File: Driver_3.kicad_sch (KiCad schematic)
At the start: 34 parts

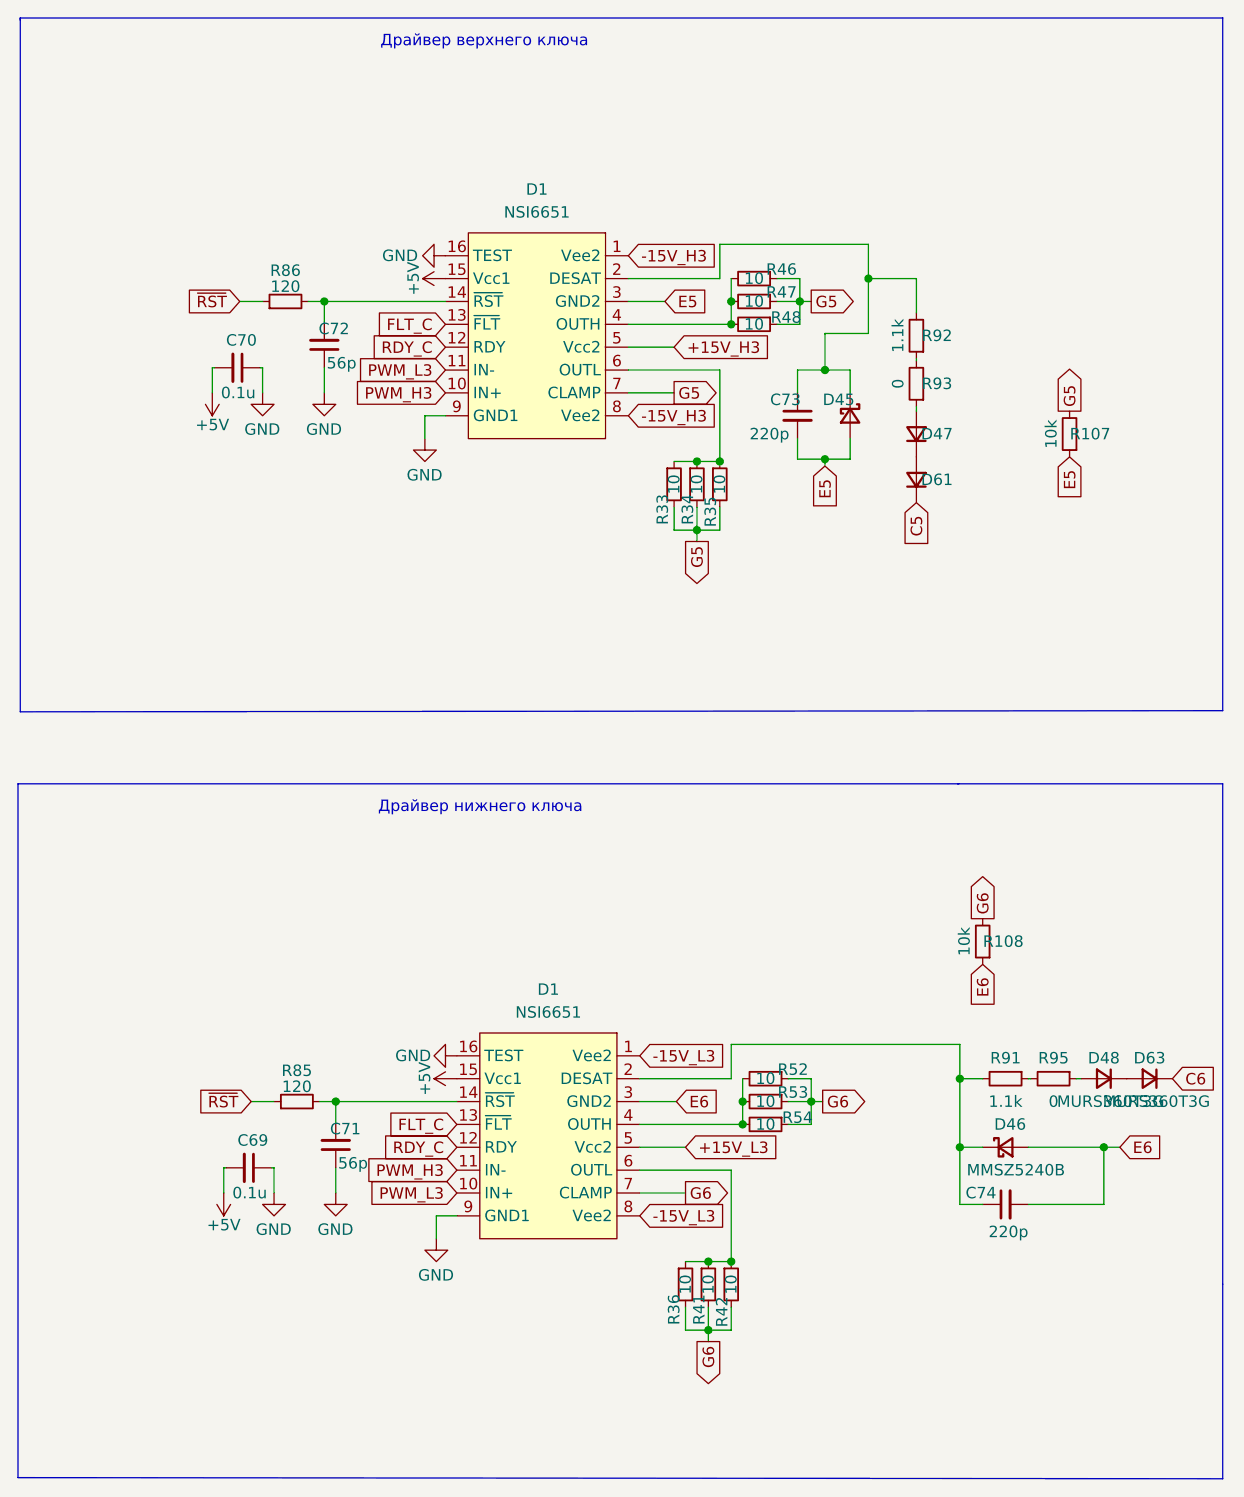
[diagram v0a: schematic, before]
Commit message: Отправил на проверку в резонит: изменил BOM
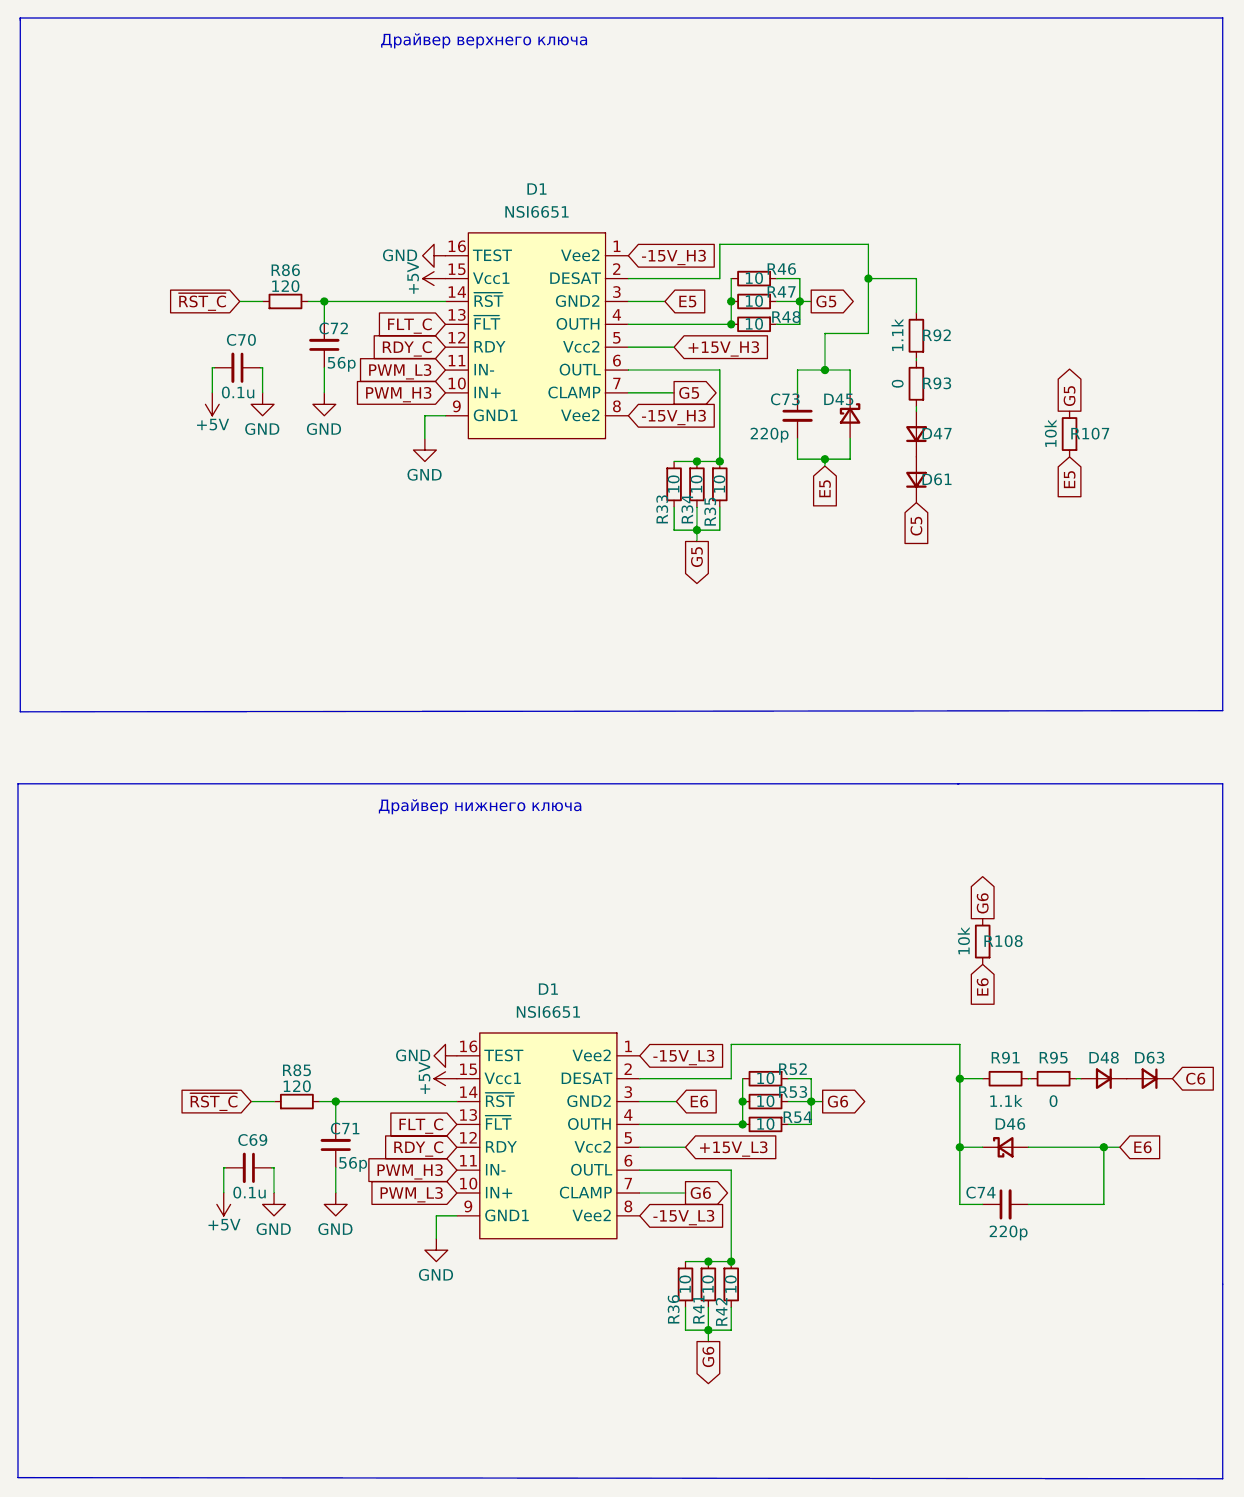
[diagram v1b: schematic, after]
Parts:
- D47, D48, D61, D63: value MURS360T3G -> MURS160
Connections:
- net ~{RST} renamed ~{RST_C}
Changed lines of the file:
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@@
 		)
 	)
-	(global_label "~{RST}"
-		(shape input)
-		(at 55.88 54.61 180)
-		(fields_autoplaced yes)
-		(effects
-			(font
-				(size 1.27 1.27)
-			)
-			(justify right)
-		)
-		(property "Intersheetrefs" "${INTERSHEET_REFS}"
-			(at 50.065 54.61 0)
-			(effects
-				(font
-					(size 1.27 1.27)
-				)
-				(justify right)
-				(hide yes)
-			)
-		)
-	)
 	(global_label "G6"
 		(shape output)
@@
 		)
 	)
-	(global_label "~{RST}"
-		(shape input)
-		(at 57.15 143.51 180)
-		(fields_autoplaced yes)
-		(effects
-			(font
-				(size 1.27 1.27)
-			)
-			(justify right)
-		)
-		(property "Intersheetrefs" "${INTERSHEET_REFS}"
-			(at 51.335 143.51 0)
-			(effects
-				(font
-					(size 1.27 1.27)
-				)
-				(justify right)
-				(hide yes)
-			)
-		)
-	)
 	(global_label "-15V_L3"
 		(shape input)
@@
 		)
 	)
+	(global_label "~{RST_C}"
+		(shape input)
+		(at 55.88 54.61 180)
+		(fields_autoplaced yes)
+		(effects
+			(font
+				(size 1.27 1.27)
+			)
+			(justify right)
+		)
+		(property "Intersheetrefs" "${INTERSHEET_REFS}"
+			(at 47.2101 54.61 0)
+			(effects
+				(font
+					(size 1.27 1.27)
+				)
+				(justify right)
+				(hide yes)
+			)
+		)
+	)
 	(global_label "PWM_H3"
 		(shape input)
@@
 		)
 	)
+	(global_label "~{RST_C}"
+		(shape input)
+		(at 57.15 143.51 180)
+		(fields_autoplaced yes)
+		(effects
+			(font
+				(size 1.27 1.27)
+			)
+			(justify right)
+		)
+		(property "Intersheetrefs" "${INTERSHEET_REFS}"
+			(at 48.4801 143.51 0)
+			(effects
+				(font
+					(size 1.27 1.27)
+				)
+				(justify right)
+				(hide yes)
+			)
+		)
+	)
 	(global_label "+15V_H3"
 		(shape input)
@@
 			)
 		)
-		(property "Value" "MURS360T3G"
+		(property "Value" "MURS160"
 			(at 152.654 143.51 0)
 			(effects
@@
 					(size 1.27 1.27)
 				)
+				(hide yes)
 			)
 		)
@@
 			)
 		)
-		(property "Value" "MURS360T3G"
+		(property "Value" "MURS160"
 			(at 128.524 70.104 0)
 			(effects
@@
 			)
 		)
-		(property "Value" "MURS360T3G"
+		(property "Value" "MURS160"
 			(at 157.734 143.51 0)
 			(effects
@@
 					(size 1.27 1.27)
 				)
+				(hide yes)
 			)
 		)
@@
 				)
 				(justify left)
+				(hide yes)
 			)
 		)
@@
 			)
 		)
-		(property "Value" "MURS360T3G"
+		(property "Value" "MURS160"
 			(at 128.524 75.184 0)
 			(effects

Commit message: Изменения: обновил BOM и названия в схеме
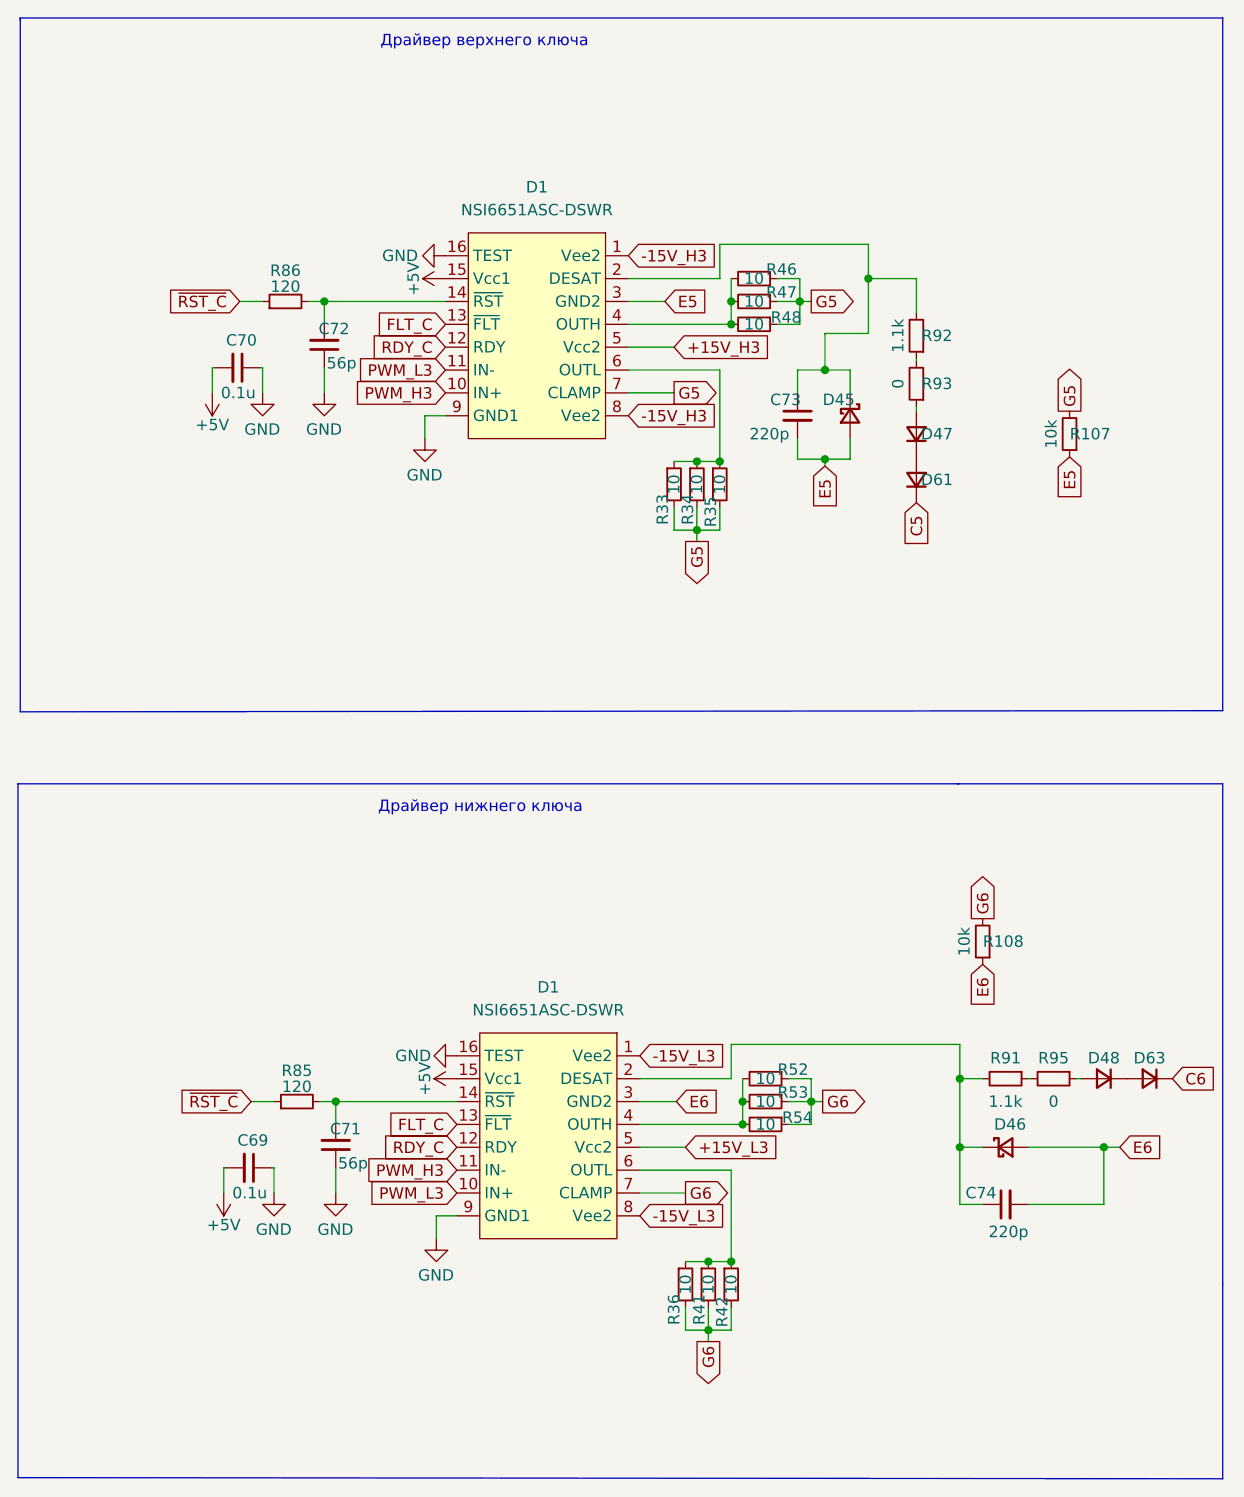
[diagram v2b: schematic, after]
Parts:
- D1: value NSI6651 -> NSI6651ASC-DSWR
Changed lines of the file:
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@@
 		(fields_autoplaced yes)
 		(property "Reference" "D1"
-			(at 88.9 42.164 0)
+			(at 88.9 41.91 0)
 			(effects
 				(font
@@
 			)
 		)
-		(property "Value" "NSI6651"
-			(at 88.9 44.704 0)
+		(property "Value" "NSI6651ASC-DSWR"
+			(at 88.9 44.45 0)
 			(effects
 				(font
@@
 		(fields_autoplaced yes)
 		(property "Reference" "D1"
-			(at 90.17 131.064 0)
+			(at 90.17 130.81 0)
 			(effects
 				(font
@@
 			)
 		)
-		(property "Value" "NSI6651"
-			(at 90.17 133.604 0)
+		(property "Value" "NSI6651ASC-DSWR"
+			(at 90.17 133.35 0)
 			(effects
 				(font

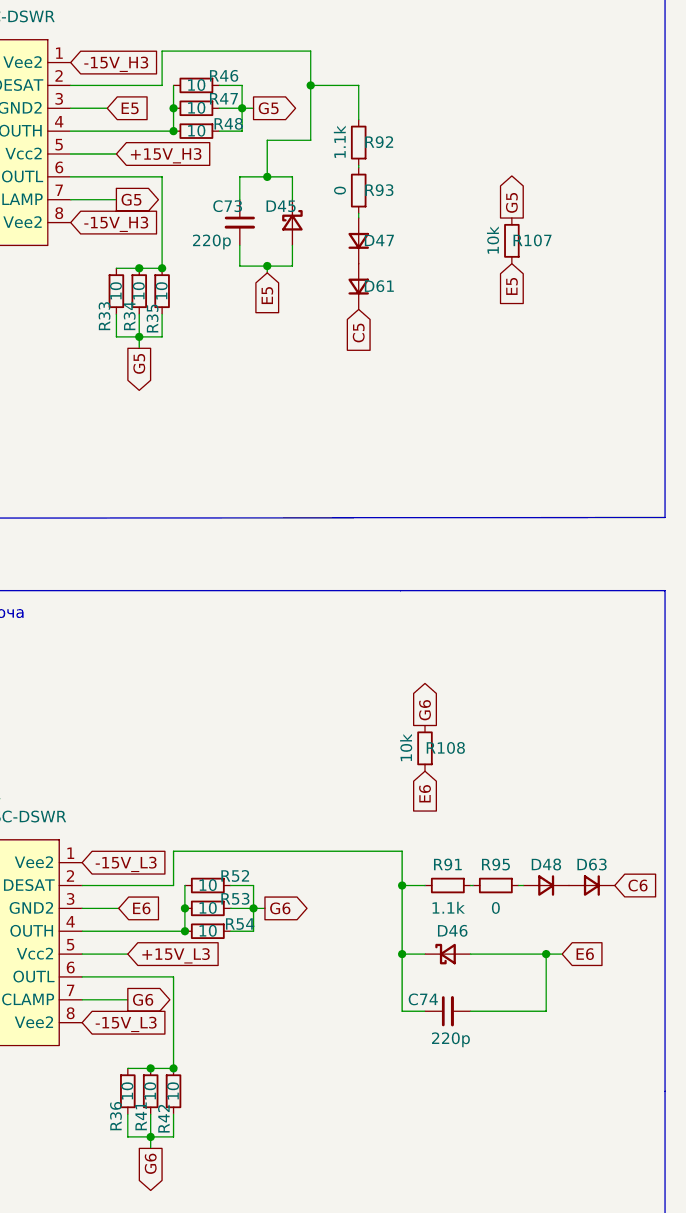
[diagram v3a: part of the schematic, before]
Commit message: Изменения: поменял трассировку полигонов, изменил трассировку цепи DESAT в фазе А
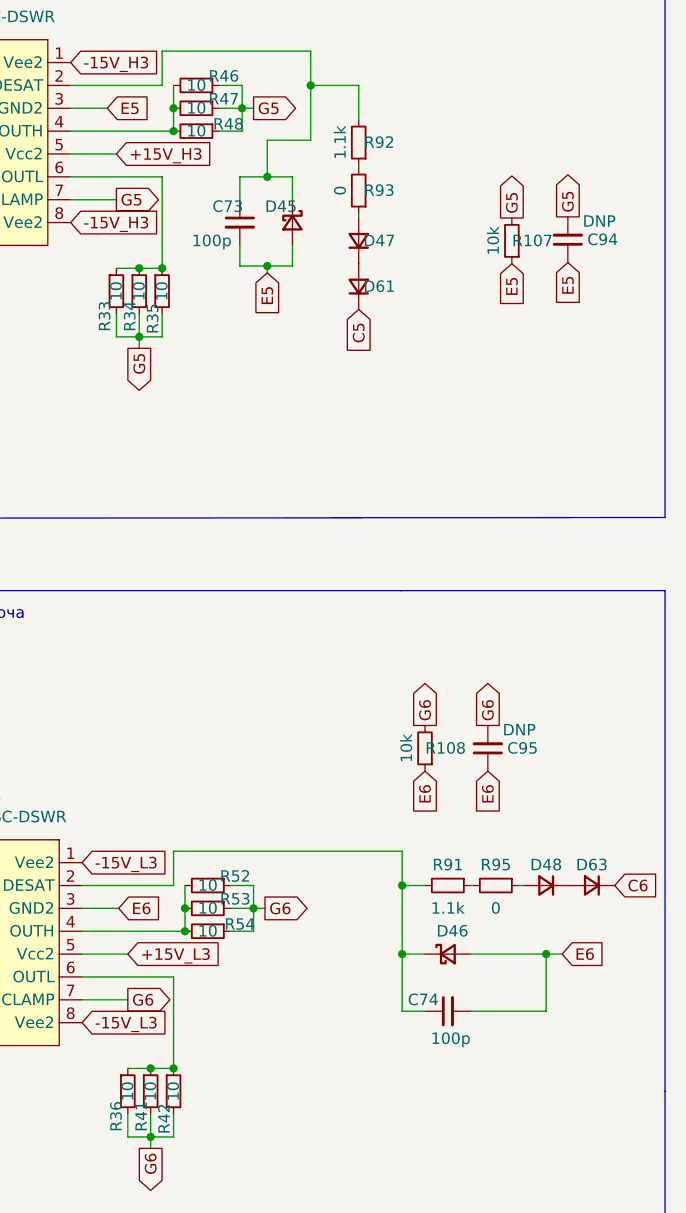
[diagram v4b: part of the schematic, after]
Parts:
- added C94, C95: DNP, Capacitor_SMD:C_0805_2012Metric_Pad1.18x1.45mm_HandSolder, symbol Device:C_Small
- C73, C74: value 220p -> 100p
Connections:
- net E5: now also C94.1
- net E6: now also C95.1
- net G5: now also C94.2
- net G6: now also C95.2
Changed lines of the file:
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@@
+		)
+	)
+	(global_label "G5"
+		(shape output)
+		(at 154.305 66.675 90)
+		(fields_autoplaced yes)
+		(effects
+			(font
+				(size 1.27 1.27)
+			)
+			(justify left)
+		)
+		(property "Intersheetrefs" "${INTERSHEET_REFS}"
+			(at 154.2256 61.7824 90)
+			(effects
+				(font
+					(size 1.27 1.27)
+				)
+				(justify left)
+				(hide yes)
+			)
 		)
 	)
@@
 		)
 	)
+	(global_label "G6"
+		(shape output)
+		(at 145.415 123.19 90)
+		(fields_autoplaced yes)
+		(effects
+			(font
+				(size 1.27 1.27)
+			)
+			(justify left)
+		)
+		(property "Intersheetrefs" "${INTERSHEET_REFS}"
+			(at 145.3356 118.2974 90)
+			(effects
+				(font
+					(size 1.27 1.27)
+				)
+				(justify left)
+				(hide yes)
+			)
+		)
+	)
 	(global_label "RDY_C"
 		(shape input)
@@
 		)
 	)
+	(global_label "E5"
+		(shape input)
+		(at 154.305 71.755 270)
+		(fields_autoplaced yes)
+		(effects
+			(font
+				(size 1.27 1.27)
+			)
+			(justify right)
+		)
+		(property "Intersheetrefs" "${INTERSHEET_REFS}"
+			(at 154.2256 76.5267 90)
+			(effects
+				(font
+					(size 1.27 1.27)
+				)
+				(justify right)
+				(hide yes)
+			)
+		)
+	)
 	(global_label "G6"
 		(shape output)
@@
 		)
 	)
+	(global_label "E6"
+		(shape input)
+		(at 145.415 128.27 270)
+		(fields_autoplaced yes)
+		(effects
+			(font
+				(size 1.27 1.27)
+			)
+			(justify right)
+		)
+		(property "Intersheetrefs" "${INTERSHEET_REFS}"
+			(at 145.3356 133.0417 90)
+			(effects
+				(font
+					(size 1.27 1.27)
+				)
+				(justify right)
+				(hide yes)
+			)
+		)
+	)
 	(global_label "G5"
 		(shape output)
@@
 	)
 	(symbol
+		(lib_id "Device:C_Small")
+		(at 145.415 125.73 180)
+		(unit 1)
+		(exclude_from_sim no)
+		(in_bom yes)
+		(on_board yes)
+		(dnp no)
+		(property "Reference" "C95"
+			(at 151.003 125.73 0)
+			(effects
+				(font
+					(size 1.27 1.27)
+				)
+				(justify left)
+			)
+		)
+		(property "Value" "DNP"
+			(at 150.749 123.698 0)
+			(effects
+				(font
+					(size 1.27 1.27)
+				)
+				(justify left)
+			)
+		)
+		(property "Footprint" "Capacitor_SMD:C_0805_2012Metric_Pad1.18x1.45mm_HandSolder"
+			(at 145.415 125.73 0)
+			(effects
+				(font
+					(size 1.27 1.27)
+				)
+				(hide yes)
+			)
+		)
+		(property "Datasheet" "~"
+			(at 145.415 125.73 0)
+			(effects
+				(font
+					(size 1.27 1.27)
+				)
+				(hide yes)
+			)
+		)
+		(property "Description" "Unpolarized capacitor, small symbol"
+			(at 145.415 125.73 0)
+			(effects
+				(font
+					(size 1.27 1.27)
+				)
+				(hide yes)
+			)
+		)
+		(pin "1"
+		)
+		(pin "2"
+		)
+		(instances
+			(project "Adapter"
+				(path "/e63e39d7-6ac0-4ffd-8aa3-1841a4541b55/4f6bfb91-7e0a-4b8d-9918-082ff107cb6c"
+					(reference "C95")
+					(unit 1)
+				)
+			)
+		)
+	)
+	(symbol
 		(lib_id "Device:R_Small")
 		(at 105.41 163.83 0)
@@
 			)
 		)
-		(property "Value" "220p"
+		(property "Value" "100p"
 			(at 112.522 69.342 0)
 			(effects
@@
 	)
 	(symbol
+		(lib_id "Device:C_Small")
+		(at 154.305 69.215 180)
+		(unit 1)
+		(exclude_from_sim no)
+		(in_bom yes)
+		(on_board yes)
+		(dnp no)
+		(property "Reference" "C94"
+			(at 159.893 69.215 0)
+			(effects
+				(font
+					(size 1.27 1.27)
+				)
+				(justify left)
+			)
+		)
+		(property "Value" "DNP"
+			(at 159.639 67.183 0)
+			(effects
+				(font
+					(size 1.27 1.27)
+				)
+				(justify left)
+			)
+		)
+		(property "Footprint" "Capacitor_SMD:C_0805_2012Metric_Pad1.18x1.45mm_HandSolder"
+			(at 154.305 69.215 0)
+			(effects
+				(font
+					(size 1.27 1.27)
+				)
+				(hide yes)
+			)
+		)
+		(property "Datasheet" "~"
+			(at 154.305 69.215 0)
+			(effects
+				(font
+					(size 1.27 1.27)
+				)
+				(hide yes)
+			)
+		)
+		(property "Description" "Unpolarized capacitor, small symbol"
+			(at 154.305 69.215 0)
+			(effects
+				(font
+					(size 1.27 1.27)
+				)
+				(hide yes)
+			)
+		)
+		(pin "1"
+		)
+		(pin "2"
+		)
+		(instances
+			(project "Adapter"
+				(path "/e63e39d7-6ac0-4ffd-8aa3-1841a4541b55/4f6bfb91-7e0a-4b8d-9918-082ff107cb6c"
+					(reference "C94")
+					(unit 1)
+				)
+			)
+		)
+	)
+	(symbol
 		(lib_id "Driver_My:NSI6651")
 		(at 90.17 135.89 0)
@@
 			)
 		)
-		(property "Value" "220p"
+		(property "Value" "100p"
 			(at 143.51 157.988 90)
 			(effects
